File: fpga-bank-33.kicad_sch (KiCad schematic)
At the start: 1 part

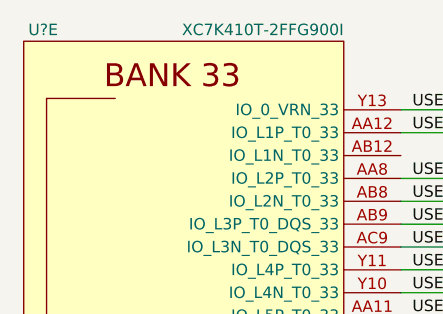
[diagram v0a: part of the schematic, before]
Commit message: Fix FPGA symbol
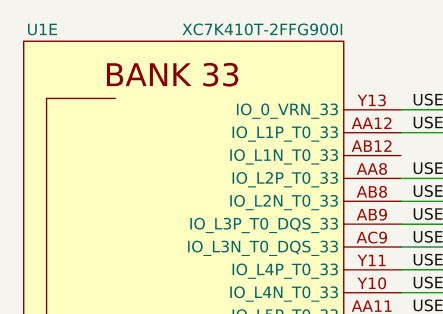
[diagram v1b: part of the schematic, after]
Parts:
- gave numbers to parts that had none: 1
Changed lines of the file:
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@@
     (effects (font (size 1.27 1.27)) (justify left))
   )
-  (symbol (lib_name "XC7K410T-2FFG900I_1") (lib_id "antmicroMicrocontrollers:XC7K410T-2FFG900I") (at 119.38 144.78 0) (unit 5)
+  (symbol (lib_id "antmicroMicrocontrollers:XC7K410T-2FFG900I") (at 119.38 144.78 0) (unit 5)
     (in_bom yes) (on_board yes)
-    (property "Reference" "U?" (id 0) (at 105.41 74.93 0)
+    (property "Reference" "U1" (id 0) (at 105.41 74.93 0)
       (effects (font (size 1.27 1.27)) (justify right))
     )

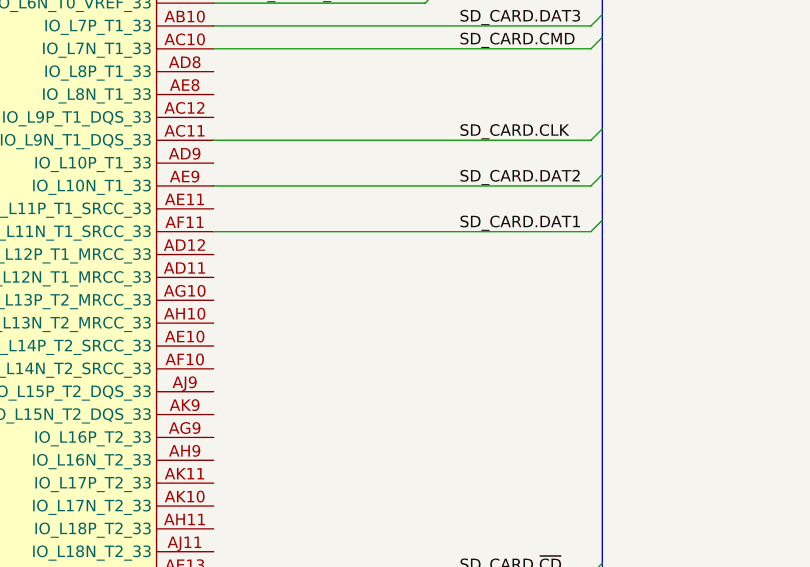
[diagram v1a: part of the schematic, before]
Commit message: Connect I2C bus
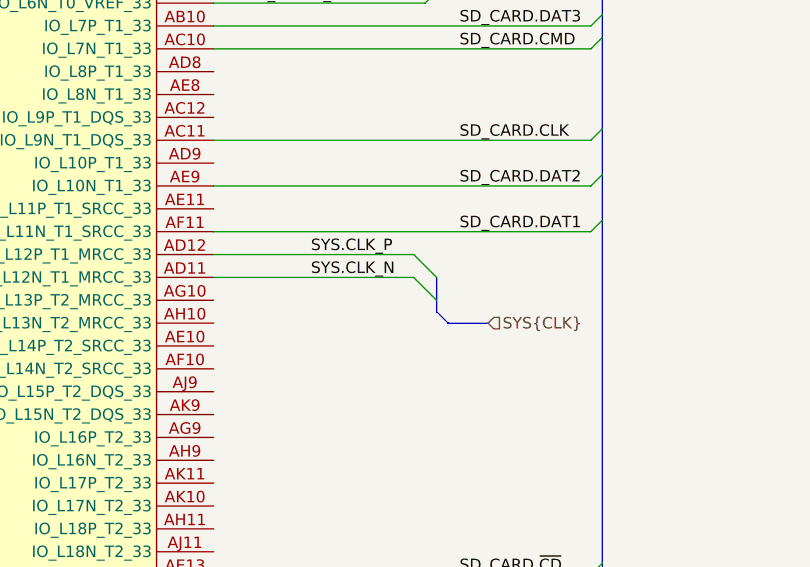
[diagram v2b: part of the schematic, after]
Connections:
- net SYS.CLK_N: now reaches U1.AD11 (IO_L12N_T1_MRCC_33)
- net SYS.CLK_P: now reaches U1.AD12 (IO_L12P_T1_MRCC_33)
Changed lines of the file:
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@@
+    (stroke (width 0) (type default) (color 0 0 0 0))
+  )
+  (bus_entry (at 168.275 144.78) (size -2.54 -2.54)
     (stroke (width 0) (type default) (color 0 0 0 0))
   )
@@
     (stroke (width 0) (type default) (color 0 0 0 0))
   )
+  (bus_entry (at 168.275 147.32) (size -2.54 -2.54)
+    (stroke (width 0) (type default) (color 0 0 0 0))
+  )
+  (bus (pts (xy 169.545 149.86) (xy 168.275 148.59))
+    (stroke (width 0) (type default) (color 0 0 0 0))
+  )
   (wire (pts (xy 185.42 129.54) (xy 143.51 129.54))
     (stroke (width 0) (type default) (color 0 0 0 0))
@@
     (stroke (width 0) (type default) (color 0 0 0 0))
   )
+  (bus (pts (xy 168.275 148.59) (xy 168.275 147.32))
+    (stroke (width 0) (type default) (color 0 0 0 0))
+  )
   (wire (pts (xy 167.005 180.34) (xy 143.51 180.34))
     (stroke (width 0) (type default) (color 0 0 0 0))
@@
     (stroke (width 0) (type default) (color 0 0 0 0))
   )
-  (wire (pts (xy 185.42 139.7) (xy 143.51 139.7))
+  (wire (pts (xy 143.51 139.7) (xy 185.42 139.7))
     (stroke (width 0) (type default) (color 0 0 0 0))
   )
@@
     (stroke (width 0) (type default) (color 0 0 0 0))
   )
+  (bus (pts (xy 173.99 149.86) (xy 169.545 149.86))
+    (stroke (width 0) (type default) (color 0 0 0 0))
+  )
+  (wire (pts (xy 143.51 144.78) (xy 165.735 144.78))
+    (stroke (width 0) (type default) (color 0 0 0 0))
+  )
   (bus (pts (xy 168.275 90.17) (xy 168.275 92.71))
     (stroke (width 0) (type default) (color 0 0 0 0))
   )
+  (bus (pts (xy 168.275 147.32) (xy 168.275 144.78))
+    (stroke (width 0) (type default) (color 0 0 0 0))
+  )
   (wire (pts (xy 168.275 181.61) (xy 168.275 186.69))
     (stroke (width 0) (type default) (color 0 0 0 0))
   )
+  (wire (pts (xy 143.51 142.24) (xy 165.735 142.24))
+    (stroke (width 0) (type default) (color 0 0 0 0))
+  )
   (wire (pts (xy 185.42 182.88) (xy 143.51 182.88))
     (stroke (width 0) (type default) (color 0 0 0 0))
@@
     (stroke (width 0) (type default) (color 0 0 0 0))
   )
+  (label "SYS.CLK_N" (at 154.305 144.78 0)
+    (effects (font (size 1.27 1.27)) (justify left bottom))
+  )
   (label "SD_CARD.DAT0" (at 170.815 182.88 0)
     (effects (font (size 1.27 1.27)) (justify left bottom))
@@
   )
   (label "USER_IO.BUTTON2" (at 144.78 104.14 0)
+    (effects (font (size 1.27 1.27)) (justify left bottom))
+  )
+  (label "SYS.CLK_P" (at 154.305 142.24 0)
     (effects (font (size 1.27 1.27)) (justify left bottom))
   )
@@
     (effects (font (size 1.27 1.27)) (justify left))
   )
+  (hierarchical_label "SYS{CLK}" (shape input) (at 173.99 149.86 0)
+    (effects (font (size 1.27 1.27)) (justify left))
+  )

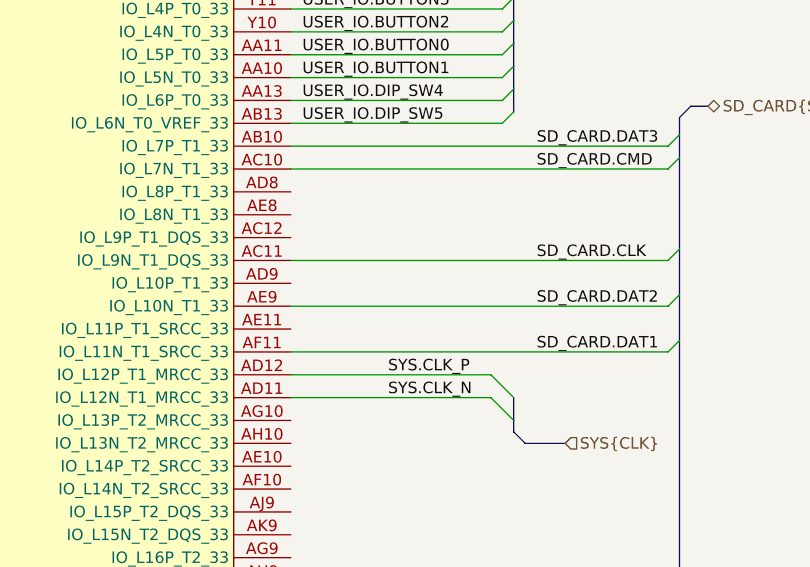
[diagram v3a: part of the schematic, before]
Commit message: Removed ToDo notes which are already done, corrected USB DET and PEN signal mapping on FPGA side, connected 200MHz generator ENA signal to FPGA
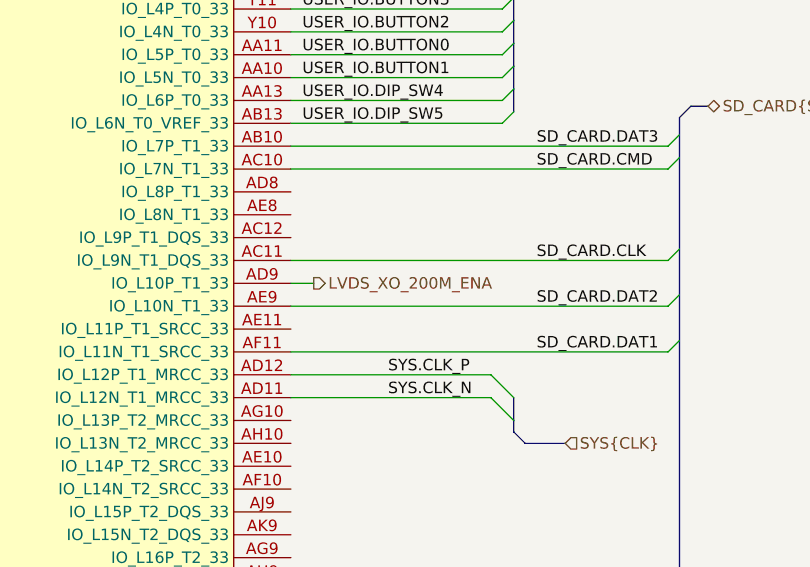
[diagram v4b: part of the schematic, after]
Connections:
- net LVDS_XO_200M_ENA: now reaches U1.AD9 (IO_L10P_T1_33)
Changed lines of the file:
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@@
+    (stroke (width 0) (type default) (color 0 0 0 0))
+  )
+  (wire (pts (xy 143.51 132.08) (xy 146.05 132.08))
     (stroke (width 0) (type default) (color 0 0 0 0))
   )
@@
     (effects (font (size 1.27 1.27)) (justify left))
   )
+  (hierarchical_label "LVDS_XO_200M_ENA" (shape output) (at 146.05 132.08 0)
+    (effects (font (size 1.27 1.27)) (justify left))
+  )

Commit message: Loclib
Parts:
- U1: footprint antmicro-footprints:xc7k410t-2ffg900I -> K410T-devboard-footprints:xc7k410t-2ffg900I; symbol antmicroMicrocontrollers:XC7K410T-2FFG900I -> K410T-devboard:XC7K410T-2FFG900I
